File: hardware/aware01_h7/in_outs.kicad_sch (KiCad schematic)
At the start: 35 parts, among them J3 InR, J4 InR, J7 OutL, J8 OutL, U3 NE5532, U4 NE5532, U5 NE5532, U7 NE5532

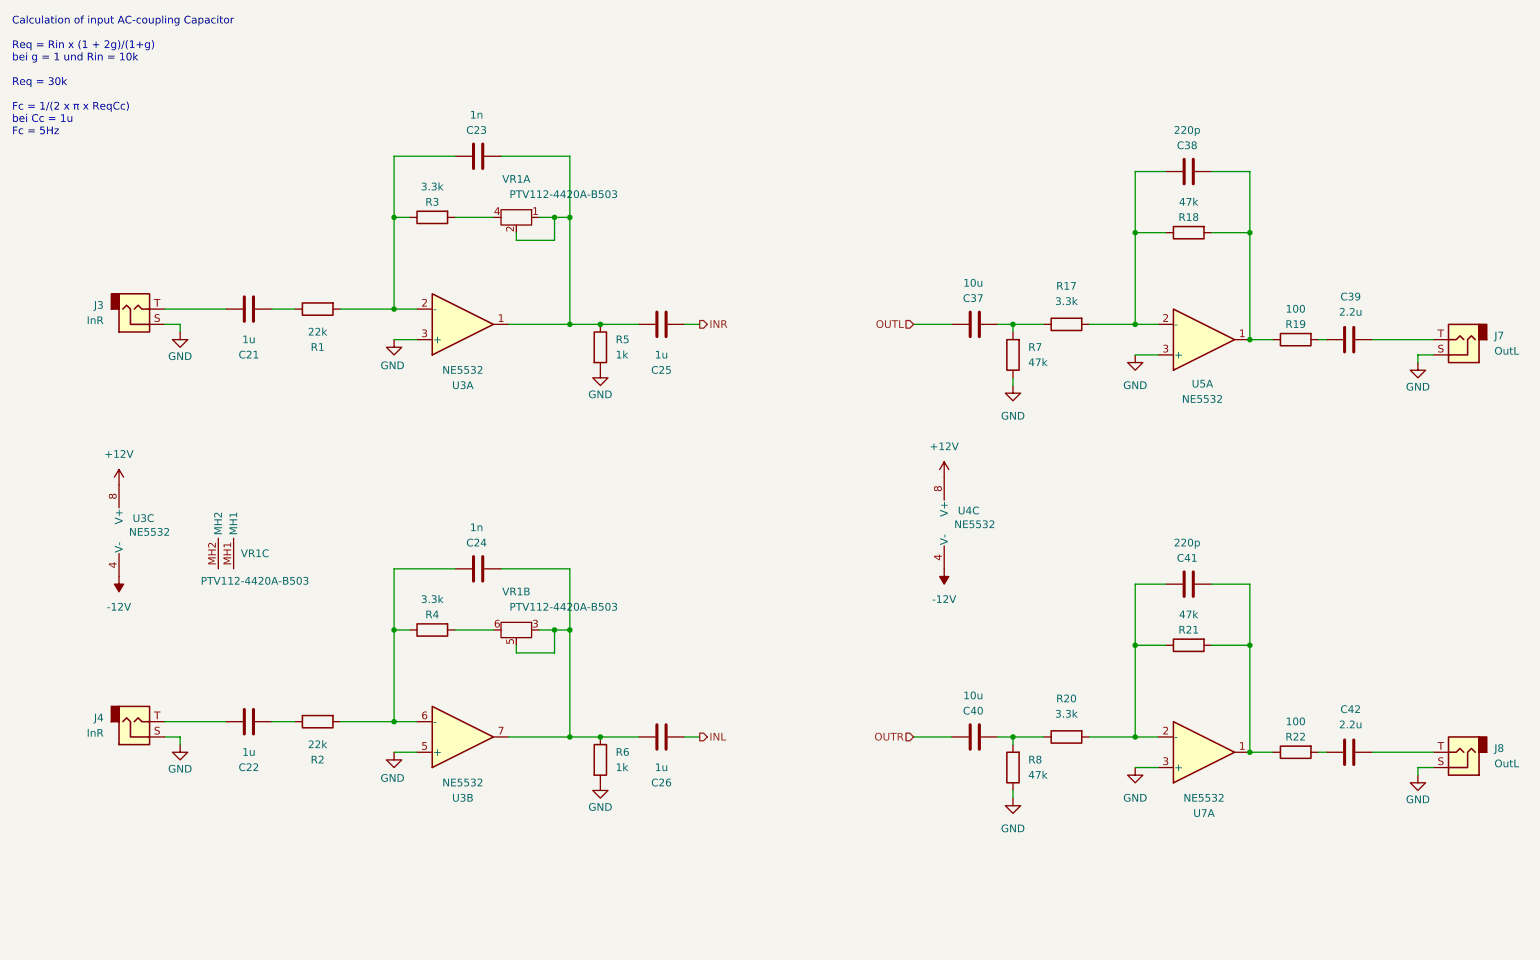
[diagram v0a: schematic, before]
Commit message: migrate to stm32h7 mcu
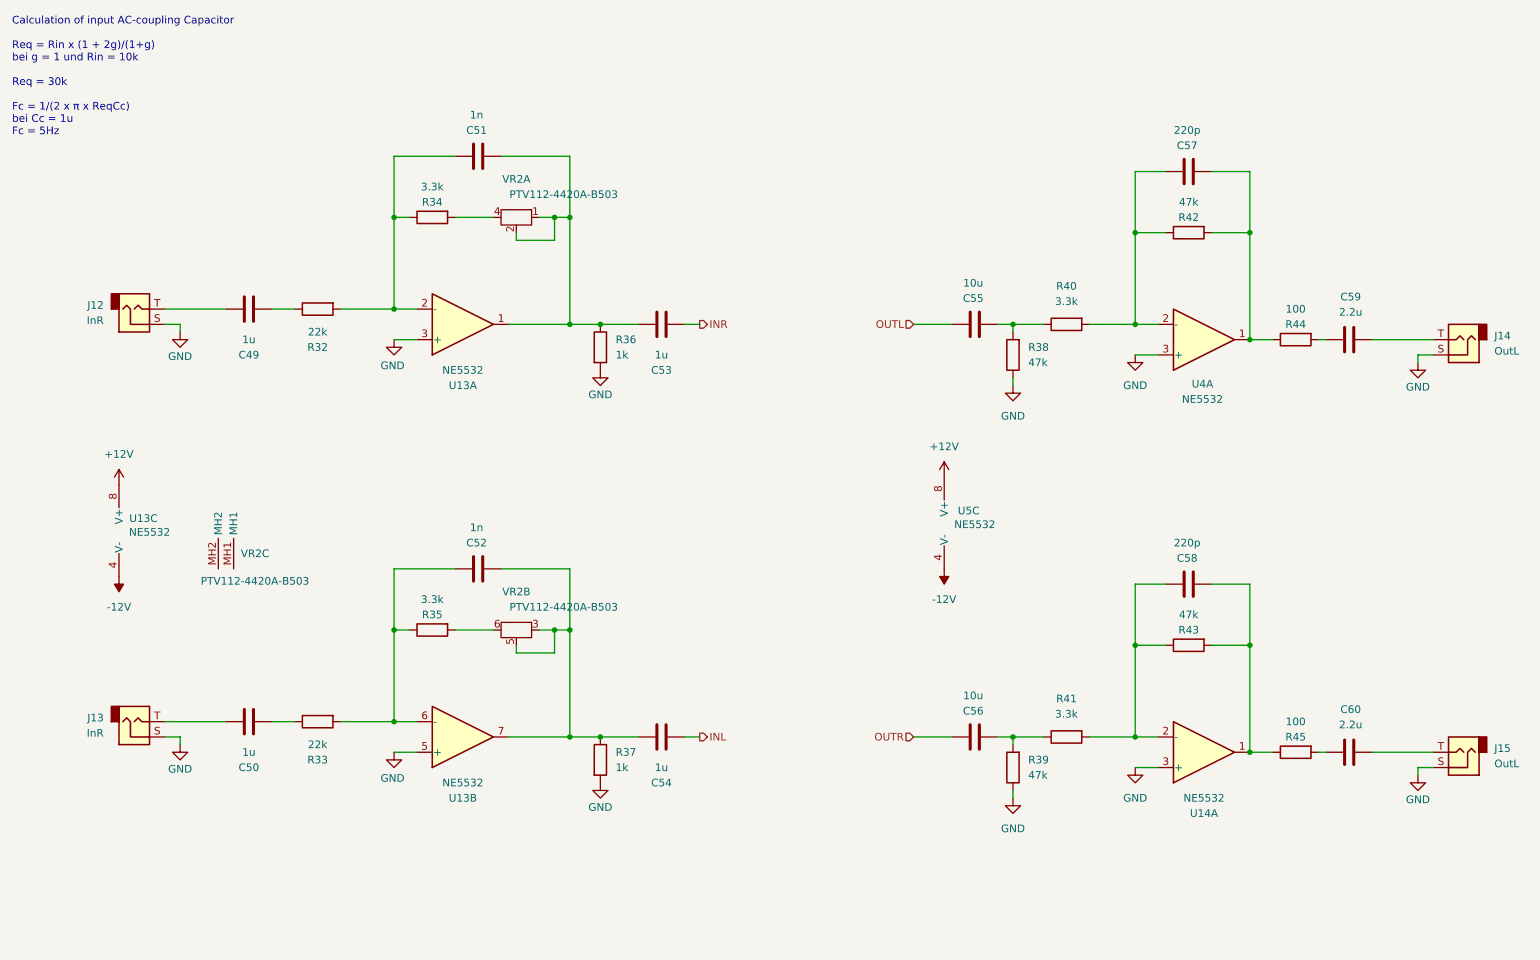
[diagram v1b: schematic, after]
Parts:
- renumbered C21 to C49, C22 to C50, C23 to C51, C24 to C52, C25 to C53, C26 to C54, C37 to C55, C40 to C56, C38 to C57, C41 to C58, C39 to C59, C42 to C60, J3 to J12, J4 to J13, J7 to J14, J8 to J15, R1 to R32, R2 to R33, R3 to R34, R4 to R35, R5 to R36, R6 to R37, R7 to R38, R8 to R39, R17 to R40, R20 to R41, R18 to R42, R21 to R43, R19 to R44, R22 to R45, U3 to U13, U7 to U14, U5 to U4, U4 to U5, VR1 to VR2

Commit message: update schematic
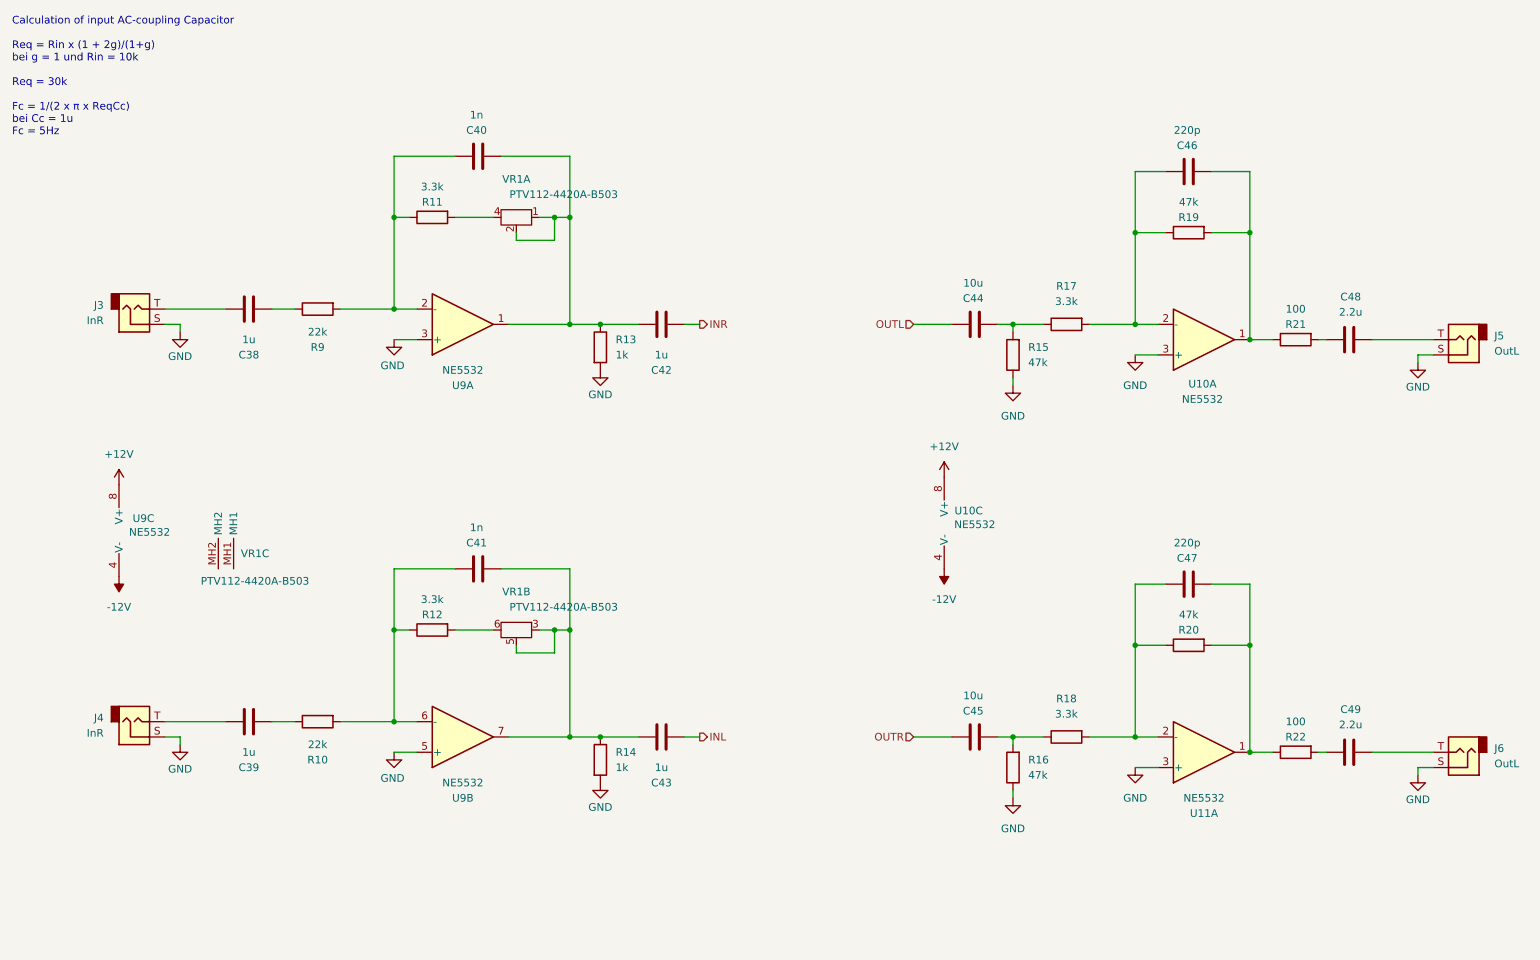
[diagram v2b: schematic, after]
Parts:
- renumbered C49 to C38, C50 to C39, C51 to C40, C52 to C41, C53 to C42, C54 to C43, C55 to C44, C56 to C45, C57 to C46, C58 to C47, C59 to C48, C60 to C49, J12 to J3, J13 to J4, J14 to J5, J15 to J6, R33 to R10, R34 to R11, R35 to R12, R36 to R13, R37 to R14, R38 to R15, R39 to R16, R40 to R17, R41 to R18, R42 to R19, R43 to R20, R44 to R21, R45 to R22, R32 to R9, U5 to U10, U4 to U10, U14 to U11, U13 to U9, VR2 to VR1

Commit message: refine schematic
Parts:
- removed C38, C39: 1u, symbol Device:C
- removed C48, C49: 2.2u, symbol Device:C
- added C53, C54, C55, C56: 100n, Capacitor_SMD:C_0603_1608Metric, symbol Device:C
- C40, C41, C42, C43, C44, C45, C46, C47: footprint (none) -> Capacitor_SMD:C_0603_1608Metric
- R10, R11, R12, R13, R14, R15, R16, R17, R18, R19, R20, R9: footprint (none) -> Resistor_SMD:R_0603_1608Metric_Pad0.98x0.95mm_HandSolder
- R21, R22: value 100 -> 1k; footprint (none) -> Resistor_SMD:R_0603_1608Metric_Pad0.98x0.95mm_HandSolder
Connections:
- net +12V: now also C53.1, C55.1
- net -12V: now also C54.1, C56.1
- net GND: now also C53.2, C54.2, C55.2, C56.2
- net at J3.T: now also R9.1
- net at J5.T: now also R21.2
- net at J4.T: now also R10.1
- net at R22.2: now also J6.T
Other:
- note added: "ALL CAPS SHOULD BE NG0 ceramic caps evtl nicht 2.2u verfügbar"
- moved on the sheet: J3, J4, J5, J6, U9C, VR1C

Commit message: assign footprints
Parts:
- removed U11: NE5532, symbol Amplifier_Operational:NE5532
- added unit 2 of U10
- J4: renamed from J3; footprint (none) -> Eurorack:THONK_PJ398SM-12
- J5: renamed from J4; footprint (none) -> Eurorack:THONK_PJ398SM-12
- J6: renamed from J5; footprint (none) -> Eurorack:THONK_PJ398SM-12
- J7: renamed from J6; footprint (none) -> Eurorack:THONK_PJ398SM-12
- U10, U9: value NE5532 -> NE5532DRG4; footprint (none) -> Eurorack:NE5532DRG4; Manufacturer_Name (none) -> https://www.ti.com/lit/ds/symlink/ne5532.pdf?ts=17370223077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; Manufacturer_Part_Number (none) -> NE5532DRG4; Mouser Part Number (none) -> 595-NE5532DRG4
- renumbered C55 to C43, C56 to C44, C40 to C45, C41 to C46, C42 to C47, C43 to C48, C53 to C49, C54 to C50, C44 to C51, C45 to C52, C46 to C53, C47 to C54
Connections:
- net GND: now also U10.5 (+)
- net at C54.2, R18.2, R20.1: now also U10.6 (-)
- net at C54.1, R20.2, R22.1: now also U10.7
- no-connect marks 0 -> 2

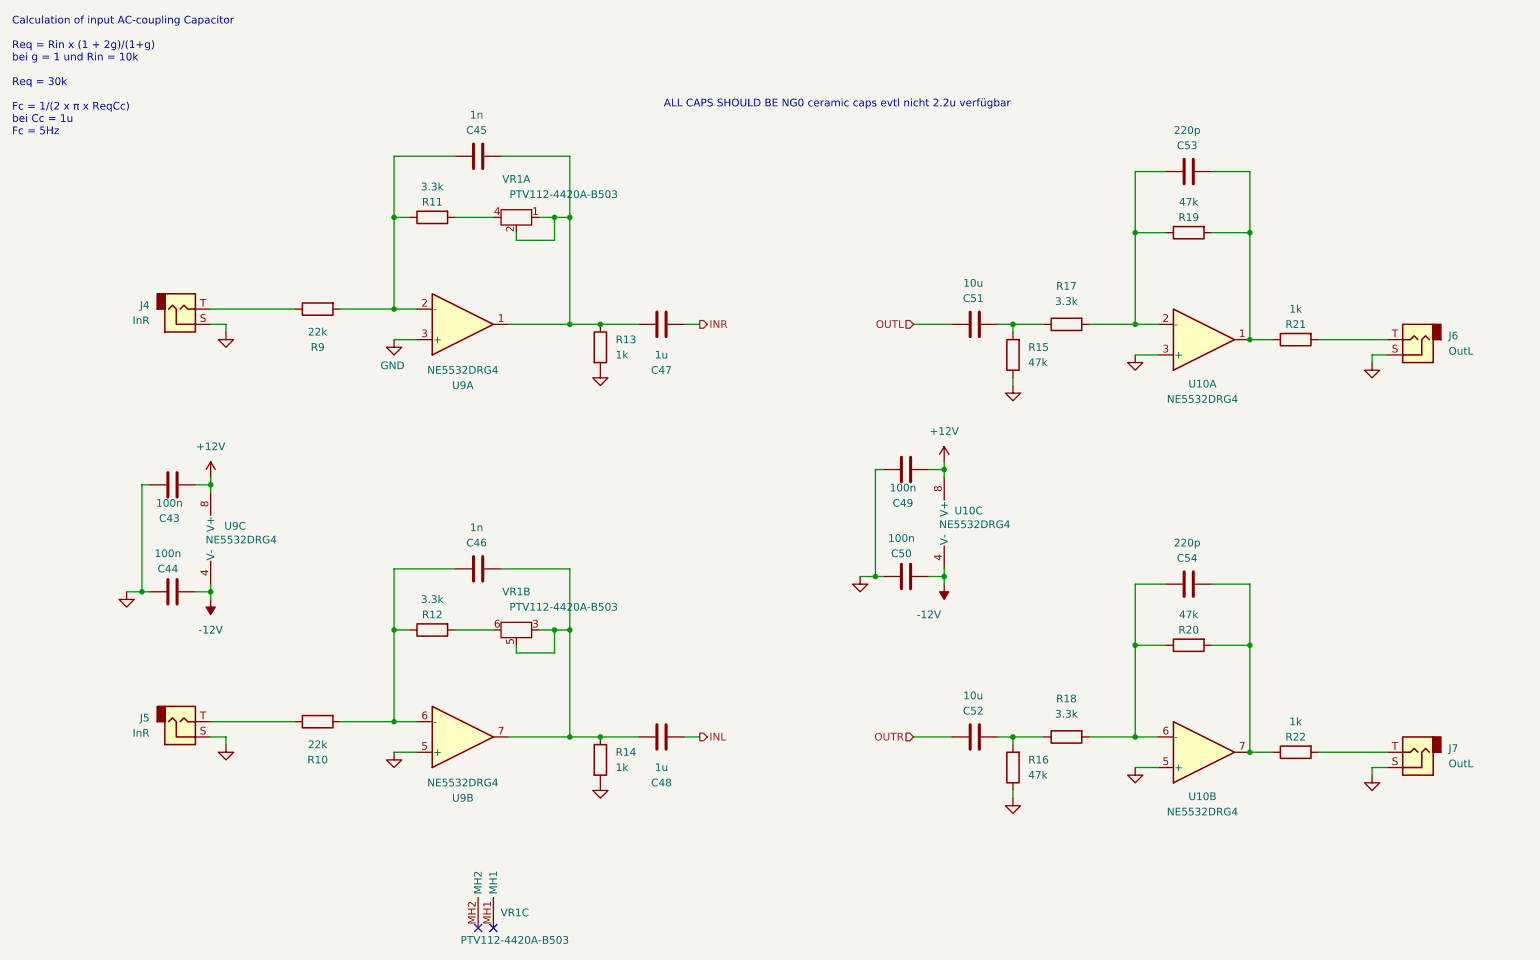
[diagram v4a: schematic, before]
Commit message: change jack symbols
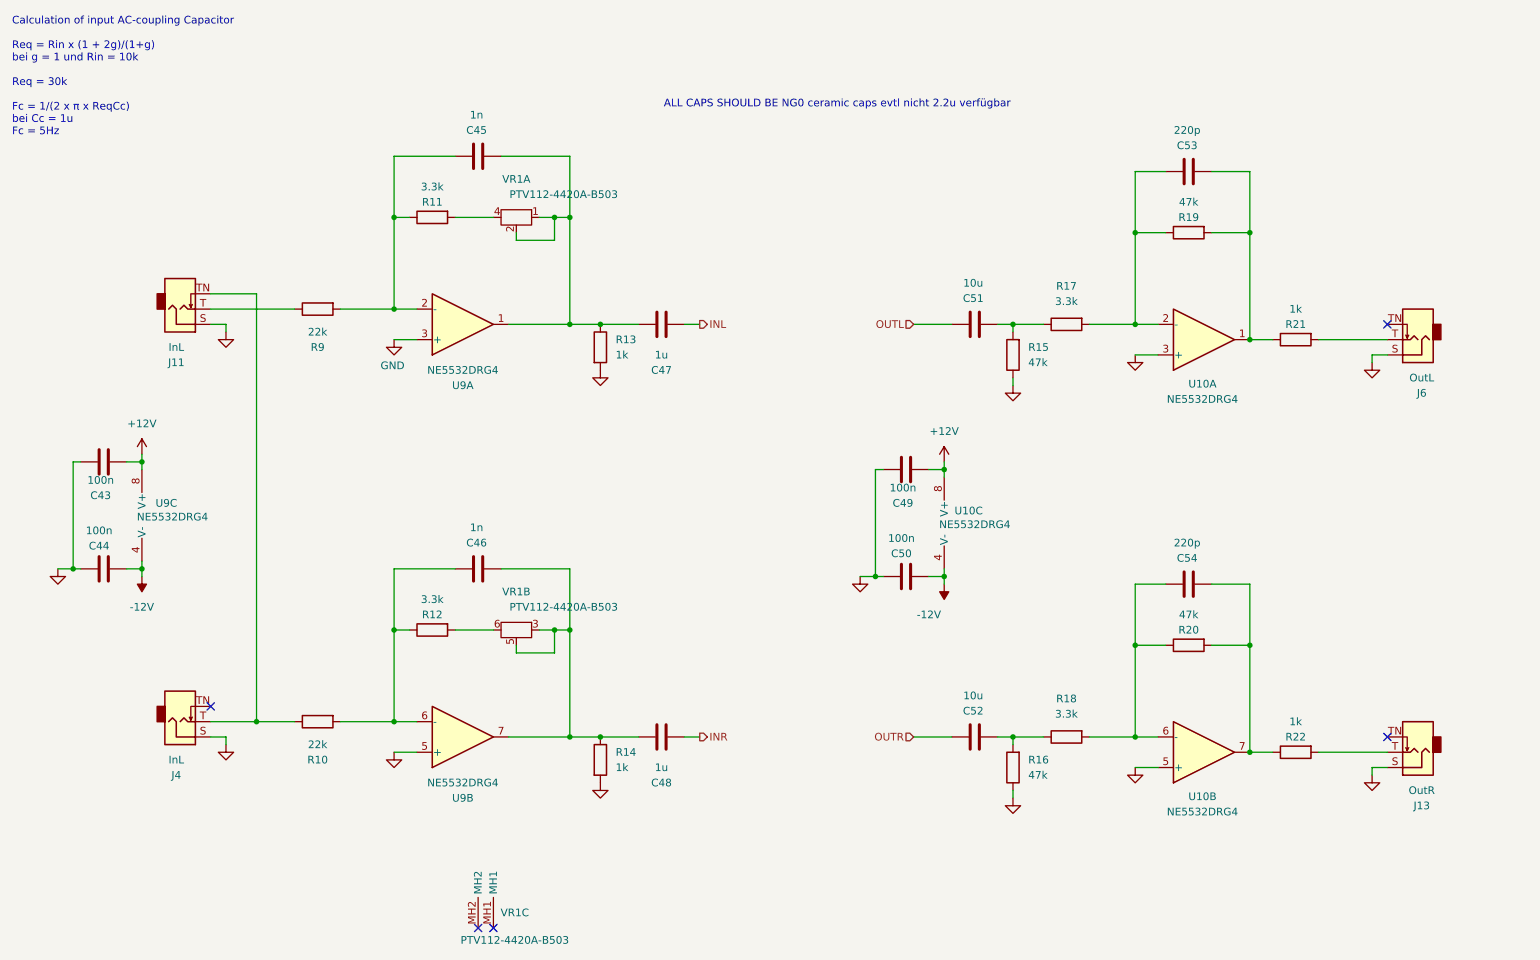
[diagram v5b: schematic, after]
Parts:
- removed J4, J5: InR, Eurorack:THONK_PJ398SM-12, symbol Connector_Audio:AudioJack2
- removed J6, J7: OutL, Eurorack:THONK_PJ398SM-12, symbol Connector_Audio:AudioJack2
- added J11, J4: InL, Connector_Audio:Jack_3.5mm_QingPu_WQP-PJ398SM_Vertical_CircularHoles, symbol Connector_Audio:AudioJack2_SwitchT
- added J13: OutR, Connector_Audio:Jack_3.5mm_QingPu_WQP-PJ398SM_Vertical_CircularHoles, symbol Connector_Audio:AudioJack2_SwitchT
- added J6: OutL, Connector_Audio:Jack_3.5mm_QingPu_WQP-PJ398SM_Vertical_CircularHoles, symbol Connector_Audio:AudioJack2_SwitchT
- VR1: footprint PTV1124420AB503 -> Eurorack:PTV1124420AB503
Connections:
- net GND: now also J11.S, J13.S, J4.S, J6.S
- net INL: now also C47.2; no longer C48.2
- net INR: now also C48.2; no longer C47.2
- net at R10.1: now also J11.TN, J4.T
- net at R9.1: now also J11.T
- net at R22.2: now also J13.T
- net at R21.2: now also J6.T
- no-connect marks 2 -> 5
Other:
- moved on the sheet: C43, C44, U9C
